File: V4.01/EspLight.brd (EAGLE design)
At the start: 49.2 x 59 mm, 25 parts, among them IC2 LM2596T, Q1 STP16NF06L, Q2 STP16NF06L, Q3 STP16NF06L

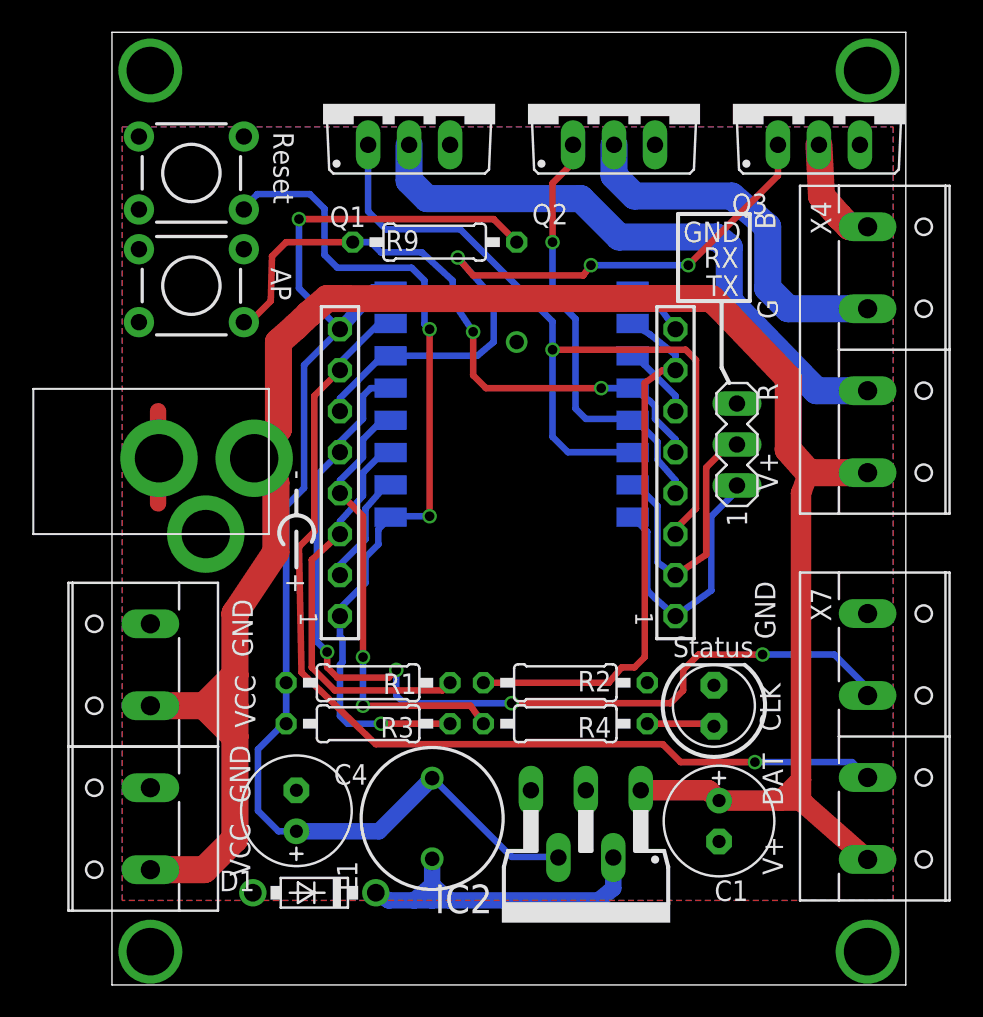
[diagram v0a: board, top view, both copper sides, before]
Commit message: V4.03 - Uploaded correct board
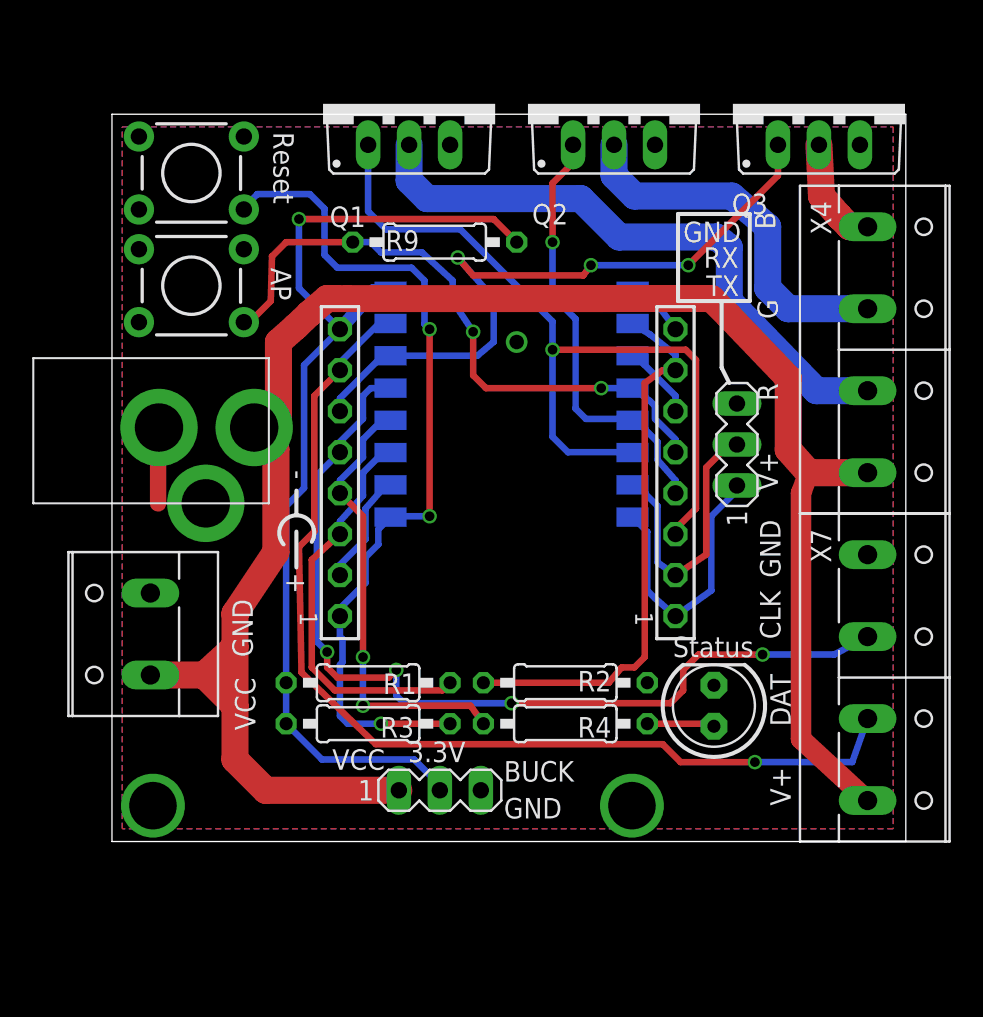
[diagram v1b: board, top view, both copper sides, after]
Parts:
- removed C1, C4: 220uF-25V, rcl:E2,5-7
- removed D1: 1N5817, diode:DO41-7.6
- removed IC2: LM2596T, national-semiconductor:T05D
- removed L1: 47uH, rcl:6000-XXXX-RC
- removed X6: (no value), con-wago-508:W237-132
- added BUCK: (no value), con-lstb:MA03-1
- moved X7 3.65 mm to (47.5, 14.6)
- moved U$1 1.91 mm to (-0.48, 30.0)
- moved X5 1.91 mm to (1.75, 17.3)
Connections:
- removed net N$15: D1.C, IC2.2, L1.1
- net +3V3: now also BUCK.2; no longer C4.+, IC2.4, L1.2
- net GND: now also BUCK.3; no longer C1.-, C4.-, D1.A, IC2.3, IC2.5, X6.2
- net V+: now also BUCK.1; no longer C1.+, IC2.1, X6.1
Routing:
- net N$15: track 22.5 -> 0.00 mm
- net +3V3: track 80.8 -> 63.4 mm
- net V+: track 133.0 -> 116.8 mm
- net GPIO13: track 62.1 -> 63.7 mm
- net GPIO14: track 59.2 -> 58.2 mm
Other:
- board size 49.2 x 59 mm -> 49.2 x 45.1 mm
- board text added: "3.3V"
